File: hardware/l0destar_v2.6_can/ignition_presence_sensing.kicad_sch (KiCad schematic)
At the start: 5 parts

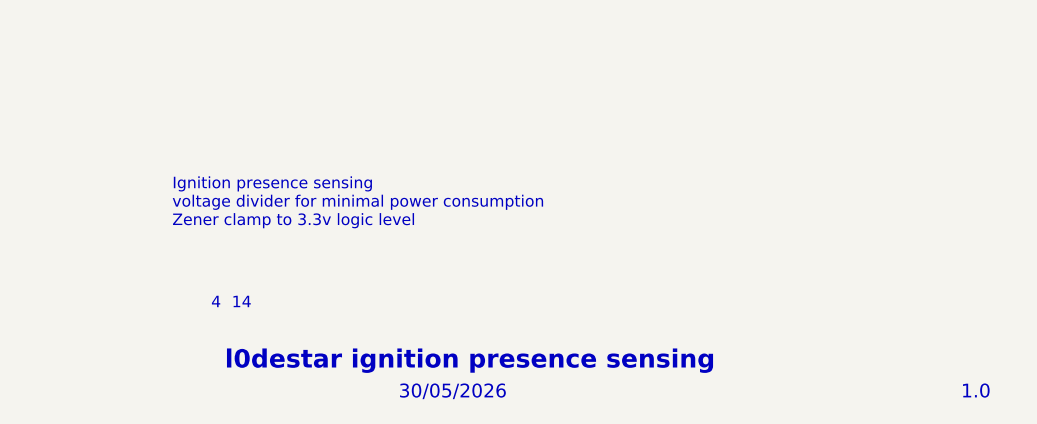
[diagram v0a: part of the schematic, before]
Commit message: fix sheet annotations
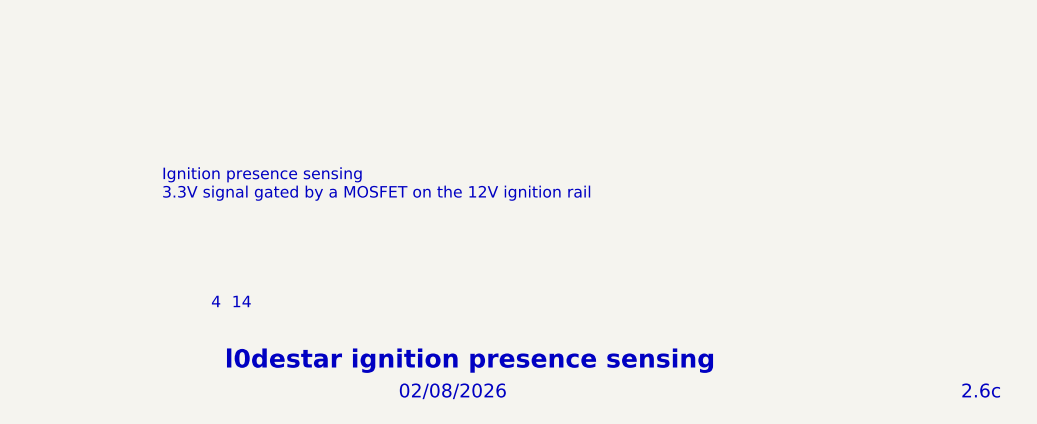
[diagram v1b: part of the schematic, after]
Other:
- note added: "02/08/2026"
- note added: "2.6c"
- note added: "Ignition presence sensing 3.3V signal gated by a MOSFET on the 12V ignition rail"
- note removed: "1.0"
- note removed: "30/05/2026"
- note removed: "Ignition presence sensing voltage divider for minimal power consumption Zener clamp to 3.3v logic level"
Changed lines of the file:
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@@
 	(generator_version "10.0")
 	(paper "A4")
-	(text "1.0"
+	(text "2.6c"
 		(exclude_from_sim no)
 		(at 268.478 193.294 0)
@@
 		)
 	)
-	(text "Ignition presence sensing\nvoltage divider for minimal power consumption\nZener clamp to 3.3v logic level"
+	(text "Ignition presence sensing\n3.3V signal gated by a MOSFET on the 12V ignition rail"
 		(exclude_from_sim no)
-		(at 180.848 172.212 0)
+		(at 179.705 170.18 0)
 		(effects
 			(font
@@
 		)
 	)
-	(text "30/05/2026"
+	(text "02/08/2026"
 		(exclude_from_sim no)
 		(at 205.994 193.294 0)
